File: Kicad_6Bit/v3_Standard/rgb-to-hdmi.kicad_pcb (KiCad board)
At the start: 2 copper layers, 65 x 30 mm, 41 parts, among them J2 Conn_02x01, P1 CONN_02X20, P2 Conn_02x05_Odd_Even, P3 Conn_01x06, P4 CONN_01X02, P5 Conn_01x04, SW1 SW_PUSH, SW2 SW_PUSH, SW3 SW_PUSH, SW4 SW_PUSH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

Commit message: Update 6/8 bit pcbs
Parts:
- removed  : mountinghole_1mm, MountingHole:mountinghole_1mm (x6)
- P1: footprint Connector_PinSocket_2.54mm:PinSocket_2x20_P2.54mm_Vertical -> Connector_PinSocket_2.54mm:PinSocket_2x20_P2.54mm_Vertical_Custom
- P4: footprint Connector_PinSocket_2.54mm:PinSocket_1x02_P2.54mm_Vertical -> Connector_PinSocket_2.54mm:PinSocket_1x02_P2.54mm_Vertical_Custom
- moved R4 3.81 mm to (27.2, 51.3)
- moved JP6 3.64 mm to (63.2, 45.1)
- moved D2 3.50 mm to (72.8, 52.2)
- moved ? 3.50 mm to (19.5, 51.0)
- moved ? 3.50 mm to (77.5, 28.0)
- moved ? 3.50 mm to (77.5, 51.0)
- moved ? 3.50 mm to (19.5, 28.0)
- moved C1 3.50 mm to (53.1, 45.4)
- moved C2 3.50 mm to (37.8, 36.6)
- moved C3 3.50 mm to (53.1, 33.3)
- moved C4 3.50 mm to (39.0, 45.5)
- moved J2 3.50 mm to (24.4, 47.1)
- moved JP1 3.50 mm to (62.7, 34.1)
- moved JP2 3.50 mm to (62.7, 37.1)
- moved JP3 3.50 mm to (62.7, 40.2)
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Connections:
- net /UV1 renamed /X1
- net /UV2 renamed /X2
- net /UV3 renamed /X3
- net /UV4 renamed /X4
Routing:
- net /GND: track 252.3 -> 250.9 mm
- net /GPIO27: track 53.7 -> 52.9 mm
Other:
- board text added: "X1"
- board text added: "X2"
- board text removed: "1"

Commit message: Update gerbers
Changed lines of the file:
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@@
     (tags "solder jumper open")
     (attr virtual)
-    (fp_text reference JP5 (at -2.20496 0.08976) (layer F.SilkS)
+    (fp_text reference JP5 (at -2.60084 0.02032) (layer F.SilkS)
       (effects (font (size 0.8 0.8) (thickness 0.12)))
     )
@@
     (tags "solder jumper open")
     (attr virtual)
-    (fp_text reference JP6 (at -2.182 0.08818) (layer F.SilkS)
+    (fp_text reference JP6 (at -2.65164 0.1524) (layer F.SilkS)
       (effects (font (size 0.8 0.8) (thickness 0.12)))
     )
@@
     (descr "LED, Round,  Rectangular size 3.3x2.4mm^2 diameter 1.8mm, 2 pins")
     (tags "LED Round  Rectangular size 3.3x2.4mm^2 diameter 1.8mm 2 pins")
-    (fp_text reference D1 (at 1.27 -2.26 90) (layer F.SilkS)
-      (effects (font (size 1 1) (thickness 0.15)))
+    (fp_text reference D1 (at -1.70752 0.02312) (layer F.SilkS)
+      (effects (font (size 0.8 0.8) (thickness 0.12)))
     )
     (fp_text value LED (at 1.27 2.26 90) (layer F.Fab)
@@
     (descr "LED, Round,  Rectangular size 3.3x2.4mm^2 diameter 1.8mm, 2 pins")
     (tags "LED Round  Rectangular size 3.3x2.4mm^2 diameter 1.8mm 2 pins")
-    (fp_text reference D2 (at 1.27 -2.26 90) (layer F.SilkS)
-      (effects (font (size 1 1) (thickness 0.15)))
+    (fp_text reference D2 (at -1.7126 0.05092) (layer F.SilkS)
+      (effects (font (size 0.8 0.8) (thickness 0.12)))
     )
     (fp_text value LED (at 1.27 2.26 90) (layer F.Fab)

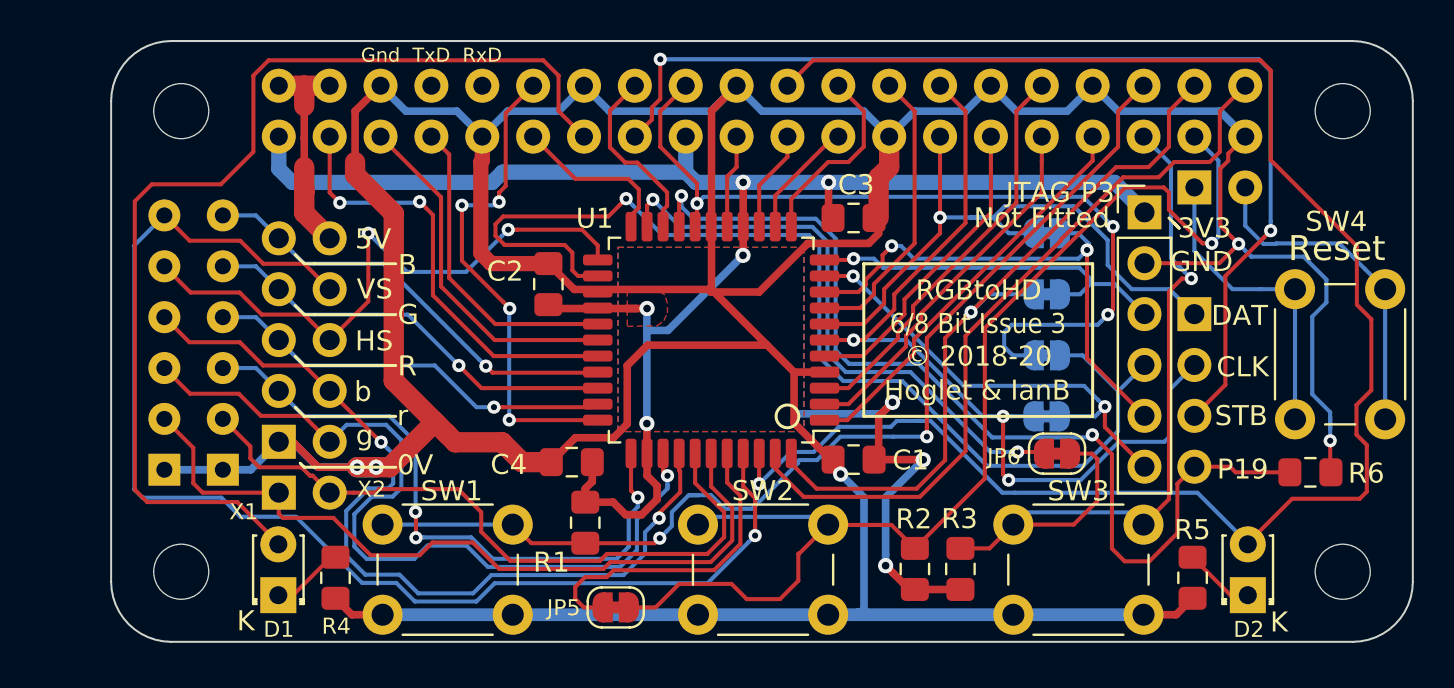
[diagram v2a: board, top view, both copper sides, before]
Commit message: Update 6/8 bit boards with identity resistor
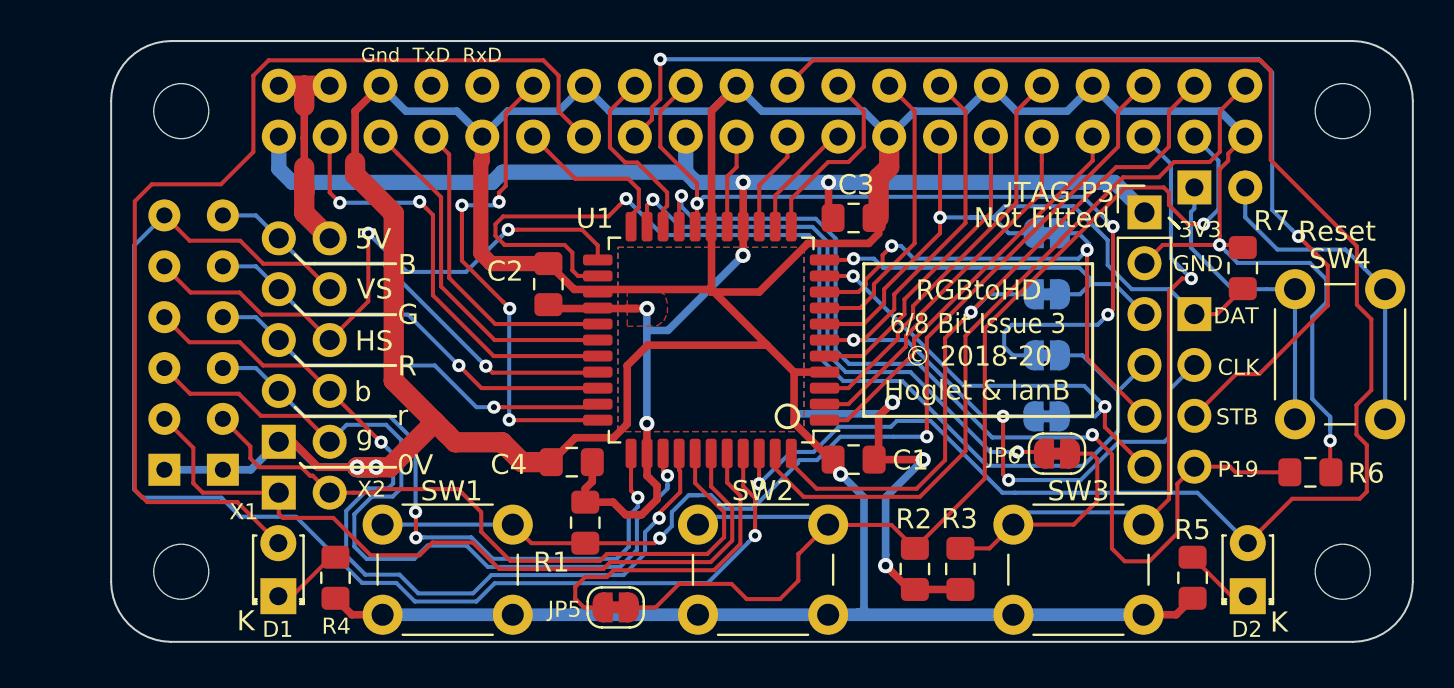
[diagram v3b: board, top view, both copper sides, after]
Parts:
- added R7: 1K, Resistor_SMD:R_0805_2012Metric_Pad1.15x1.40mm_HandSolder, F.Cu at (72.5, 35.8)
- D1, D2: footprint LED_THT:LED_D1.8mm_W3.3mm_H2.4mm -> LED_THT:LED_D1.8mm_W3.3mm_H2.4mm_Custom2
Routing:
- net /GPIO0: track 32.3 -> 35.5 mm
- net /GPIO22: track 54.4 -> 57.5 mm
- net /GPIO26: track 59.3 -> 57.5 mm
- net /GND: track 250.9 -> 251.6 mm
